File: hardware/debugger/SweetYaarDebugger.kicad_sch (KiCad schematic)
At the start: 21 parts, among them SW1 SW_DPST, U1 USBLC6-2SC6

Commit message: Add schematics
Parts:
- C1: footprint (none) -> Capacitor_SMD:C_0603_1608Metric
- C2, C4: value 4.7u -> 4.7uF; footprint (none) -> Capacitor_SMD:C_0805_2012Metric
- C3, C5: value 100n -> 100nF; footprint (none) -> Capacitor_SMD:C_0603_1608Metric
- J_PROG1: footprint (none) -> Connector_PinHeader_2.54mm:PinHeader_1x06_P2.54mm_Vertical
- R1, R_CC1, R_CC2, R_DTR1, R_RSTb1, R_RTS1, R_VBUS_DIV_BOT1, R_VBUS_DIV_TOP1: footprint (none) -> Resistor_SMD:R_0603_1608Metric
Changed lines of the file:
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@@
 			)
 		)
-		(property "Value" "100n"
+		(property "Value" "100nF"
 			(at 114.554 50.546 0)
 			(show_name no)
@@
 			)
 		)
-		(property "Footprint" ""
+		(property "Footprint" "Capacitor_SMD:C_0603_1608Metric"
 			(at 115.2652 52.07 0)
 			(hide yes)
@@
 			)
 		)
-		(property "Footprint" ""
+		(property "Footprint" "Resistor_SMD:R_0603_1608Metric"
 			(at 167.64 81.28 0)
 			(hide yes)
@@
 			)
 		)
-		(property "Footprint" ""
+		(property "Footprint" "Capacitor_SMD:C_0603_1608Metric"
 			(at 68.58 52.3748 0)
 			(hide yes)
@@
 			)
 		)
-		(property "Footprint" ""
+		(property "Footprint" "Resistor_SMD:R_0603_1608Metric"
 			(at 92.71 78.74 0)
 			(hide yes)
@@
 			)
 		)
-		(property "Footprint" ""
+		(property "Footprint" "Resistor_SMD:R_0603_1608Metric"
 			(at 106.68 62.23 0)
 			(hide yes)
@@
 			)
 		)
-		(property "Footprint" ""
+		(property "Footprint" "Resistor_SMD:R_0603_1608Metric"
 			(at 92.71 71.12 0)
 			(hide yes)
@@
 			)
 		)
-		(property "Value" "4.7u"
+		(property "Value" "4.7uF"
 			(at 106.934 50.546 0)
 			(show_name no)
@@
 			)
 		)
-		(property "Footprint" ""
+		(property "Footprint" "Capacitor_SMD:C_0805_2012Metric"
 			(at 107.6452 52.07 0)
 			(hide yes)
@@
 			)
 		)
-		(property "Footprint" ""
+		(property "Footprint" "Resistor_SMD:R_0603_1608Metric"
 			(at 207.01 62.992 90)
 			(hide yes)
@@
 			)
 		)
-		(property "Footprint" ""
+		(property "Footprint" "Connector_PinHeader_2.54mm:PinHeader_1x06_P2.54mm_Vertical"
 			(at 248.92 73.66 0)
 			(hide yes)
@@
 			)
 		)
-		(property "Footprint" ""
+		(property "Footprint" "Resistor_SMD:R_0603_1608Metric"
 			(at 49.53 53.34 0)
 			(hide yes)
@@
 			)
 		)
-		(property "Footprint" ""
+		(property "Footprint" "Resistor_SMD:R_0603_1608Metric"
 			(at 167.64 67.31 0)
 			(hide yes)
@@
 			)
 		)
-		(property "Footprint" ""
+		(property "Footprint" "Resistor_SMD:R_0603_1608Metric"
 			(at 49.53 50.8 0)
 			(hide yes)
@@
 			)
 		)
-		(property "Value" "100n"
+		(property "Value" "100nF"
 			(at 127.762 50.546 0)
 			(show_name no)
@@
 			)
 		)
-		(property "Footprint" ""
+		(property "Footprint" "Capacitor_SMD:C_0603_1608Metric"
 			(at 127.9652 52.07 0)
 			(hide yes)
@@
 			)
 		)
-		(property "Value" "4.7u"
+		(property "Value" "4.7uF"
 			(at 136.144 50.546 0)
 			(show_name no)
@@
 			)
 		)
-		(property "Footprint" ""
+		(property "Footprint" "Capacitor_SMD:C_0805_2012Metric"
 			(at 136.8552 52.07 0)
 			(hide yes)

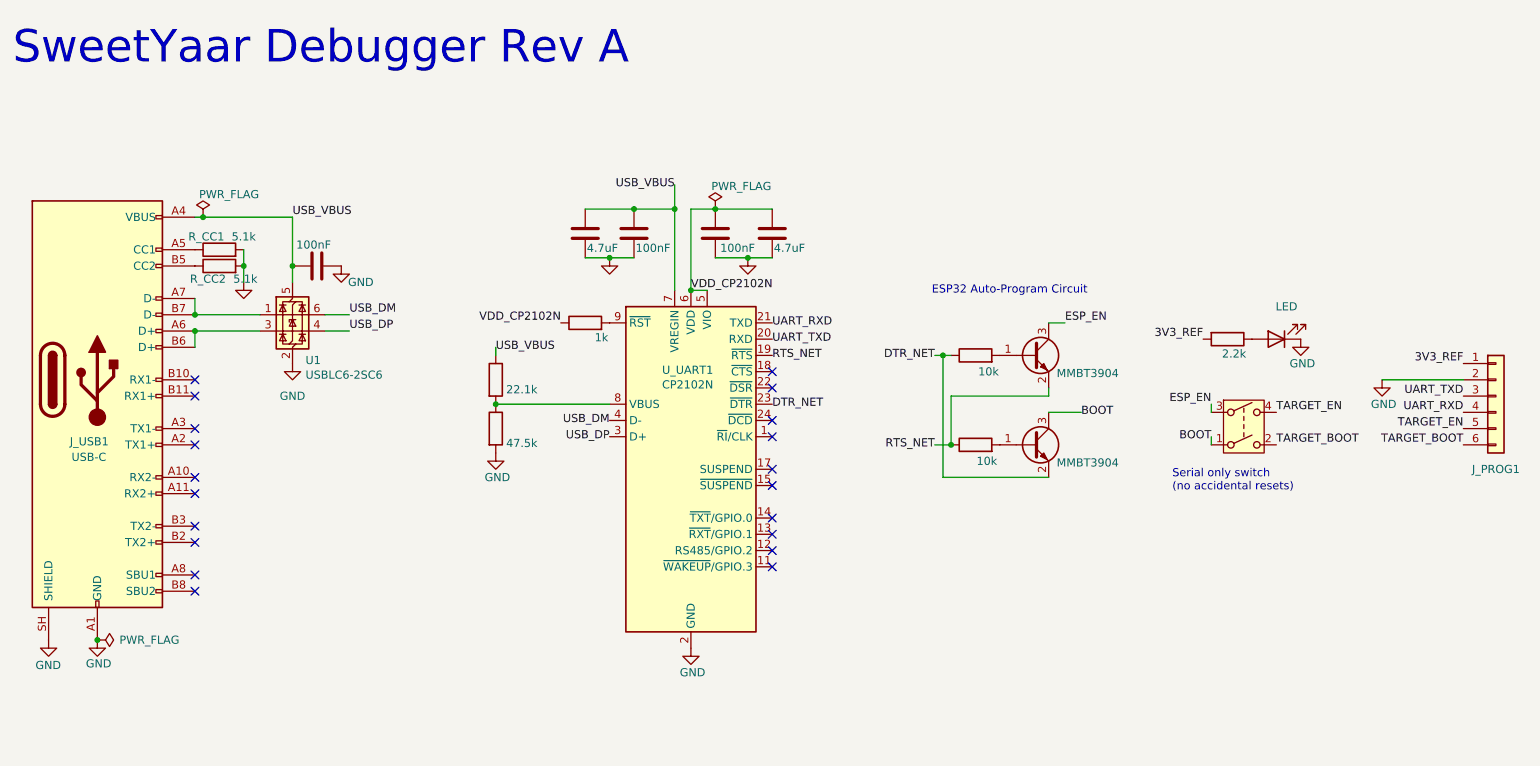
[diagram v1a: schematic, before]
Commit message: changing debugger components to match mainboard
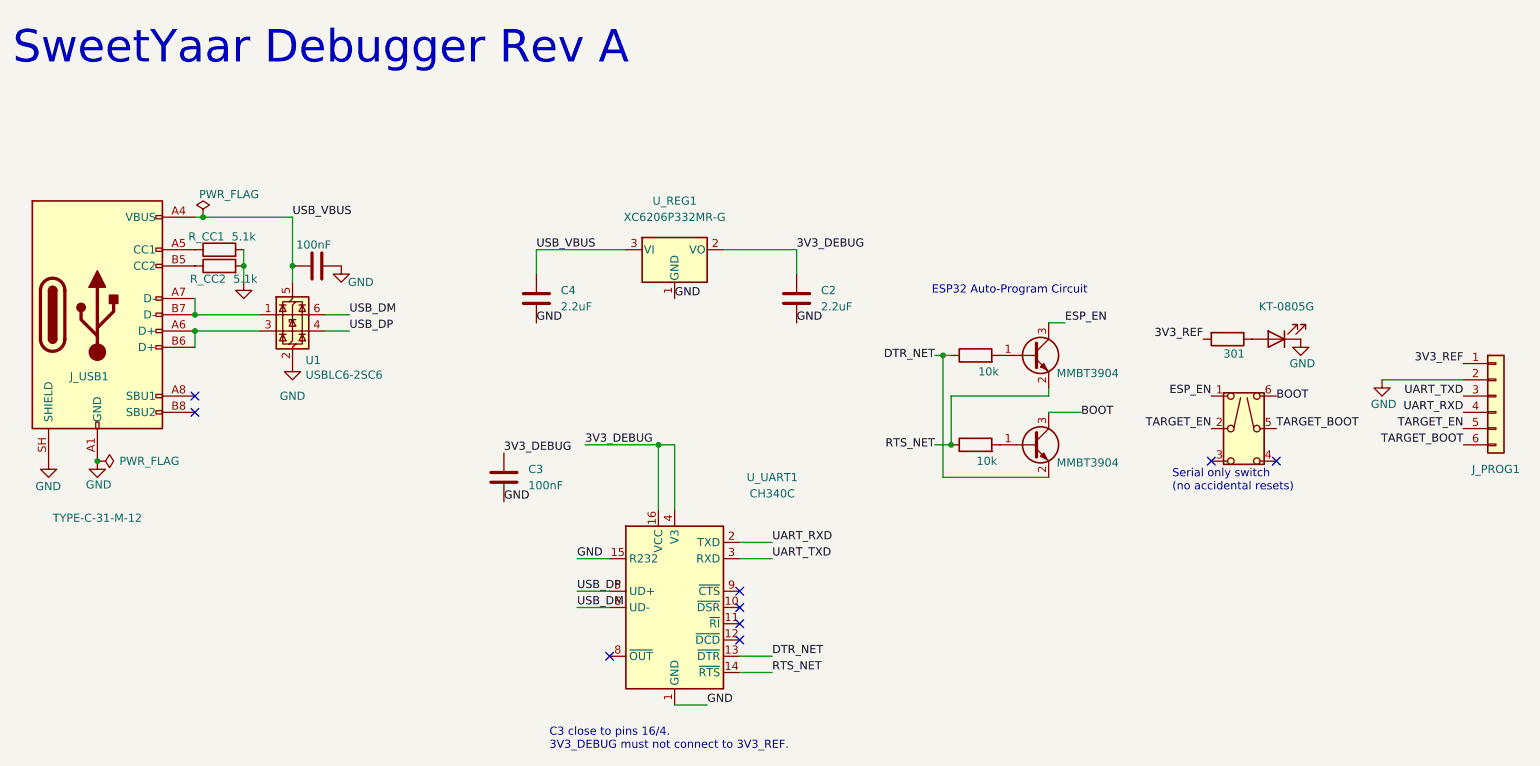
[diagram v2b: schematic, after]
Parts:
- removed C5: 100nF, Capacitor_SMD:C_0603_1608Metric, symbol Device:C
- removed R_RSTb1: 1k, Resistor_SMD:R_0603_1608Metric, symbol Device:R
- removed R_VBUS_DIV_BOT1: 47.5k, Resistor_SMD:R_0603_1608Metric, symbol Device:R
- removed R_VBUS_DIV_TOP1: 22.1k, Resistor_SMD:R_0603_1608Metric, symbol Device:R
- added U_REG1: XC6206P332MR-G, Package_TO_SOT_SMD:SOT-23-3, symbol Regulator_Linear:XC6206PxxxMR
- C1, C3: LCSC (none) -> C14663
- C2, C4: value 4.7uF -> 2.2uF; LCSC (none) -> C126591
- D1: value LED -> KT-0805G; footprint (none) -> LED_SMD:LED_0805_2012Metric; LCSC (none) -> C2297
- J_USB1: value USB-C -> TYPE-C-31-M-12; footprint (none) -> Connector_USB:USB_C_Receptacle_HRO_TYPE-C-31-M-12; symbol Connector:USB_C_Receptacle -> Connector:USB_C_Receptacle_USB2.0_16P; LCSC (none) -> C165948
- Q_DTR1, Q_RTS1: LCSC (none) -> C20526
- R1: value 2.2k -> 301; LCSC (none) -> C25192
- R_CC1, R_CC2: LCSC (none) -> C23186
- R_DTR1, R_RTS1: LCSC (none) -> C25804
- SW1: value SW_DPST -> MS-22D28-G020 (SERIAL ONLY); footprint (none) -> SweetYaar:SW-SMD_MS-22D28-G020; symbol Switch:SW_DPST -> SweetYaar:MS-22D28-G020; LCSC (none) -> C963205
- U_UART1: value CP2102N -> CH340C; footprint (none) -> Package_SO:SOIC-16_3.9x9.9mm_P1.27mm; symbol Interface_USB:CP2102N-Axx-xQFN24 -> SweetYaar:CH340C_3V3; LCSC (none) -> C7464026
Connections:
- net BOOT: now also SW1.6 (C); no longer SW1.1
- net DTR_NET: now also U_UART1.13 (~{DTR}); no longer U_UART1.23 (~{DTR})
- net ESP_EN: now also SW1.1 (A); no longer SW1.3
- net GND: now also U_UART1.1 (GND), U_UART1.15 (R232), U_REG1.1 (GND); no longer U_UART1.2 (GND), U_UART1.25 (GND)
- net RTS_NET: now also U_UART1.14 (~{RTS}); no longer U_UART1.19 (~{RTS})
- net TARGET_BOOT: now also SW1.5 (B); no longer SW1.2
- net TARGET_EN: now also SW1.2 (B); no longer SW1.4
- net UART_RXD: now also U_UART1.2 (TXD); no longer U_UART1.21 (TXD)
- net UART_TXD: now also U_UART1.3 (RXD); no longer U_UART1.20 (RXD)
- net USB_DM: now also U_UART1.6 (UD-); no longer U_UART1.4 (D-)
- net USB_DP: now also U_UART1.5 (UD+); no longer U_UART1.3 (D+)
- net USB_VBUS: now also U_REG1.3 (VI); no longer U_UART1.7 (VREGIN)
- net 3V3_DEBUG: now reaches U_UART1.16 (VCC)
- net 3V3_DEBUG: now also C2.1, C3.1, U_UART1.4 (V3), U_REG1.2 (VO)
- removed net VDD_CP2102N: C2.1, C3.1, U_UART1.5 (VIO), U_UART1.6 (VDD)
- no-connect marks 20 -> 9
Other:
- note added: "C3 close to pins 16/4. 3V3_DEBUG must not connect to 3V3_REF."

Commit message: Add routed debugger PCB and update schematic
Add the fully routed debugger board and its USB and power design rules. Update the schematic and switch documentation, including the 330 ohm LED resistor using LCSC C23138.
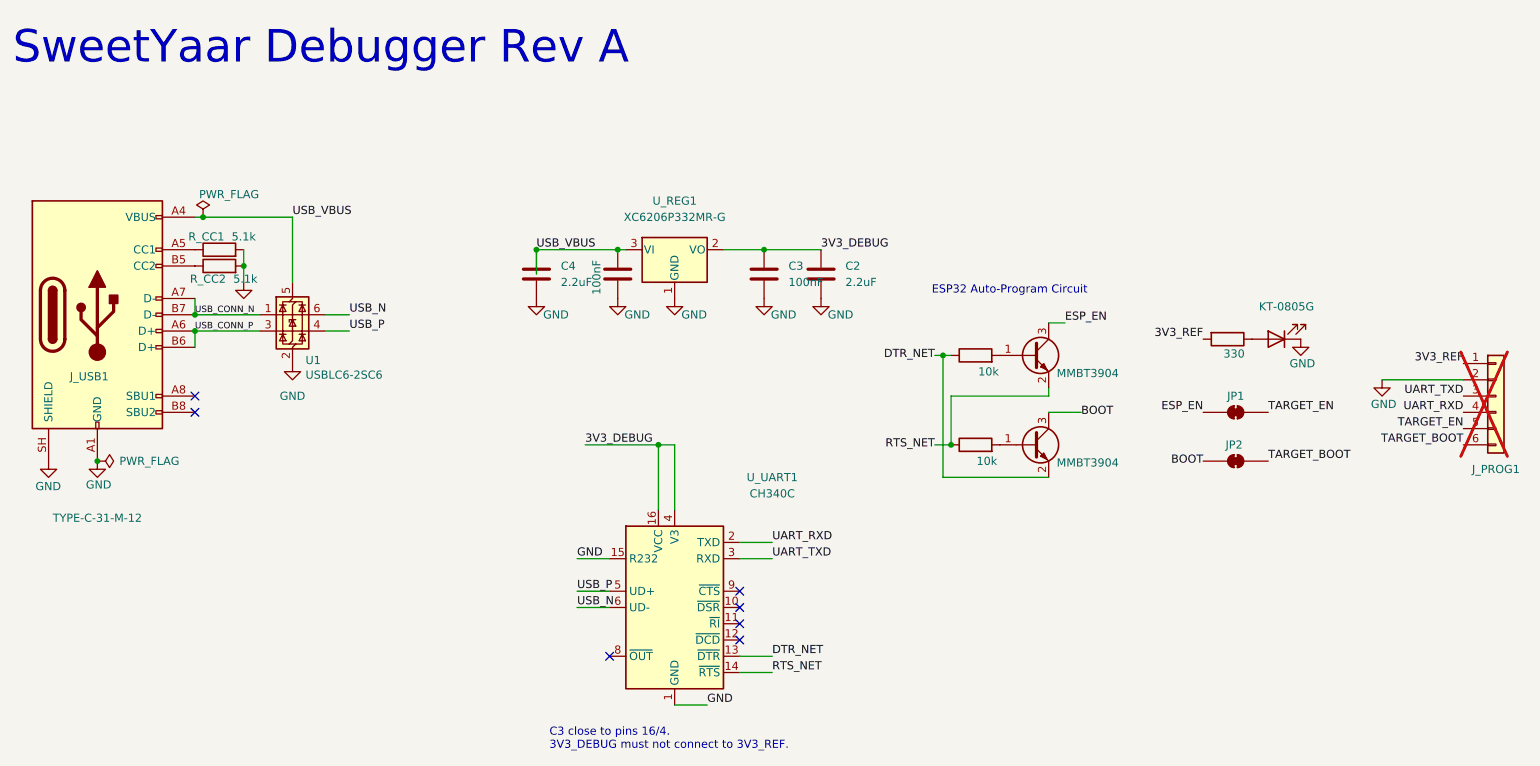
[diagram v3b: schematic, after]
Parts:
- removed SW1: MS-22D28-G020 (SERIAL ONLY), SweetYaar:SW-SMD_MS-22D28-G020, symbol SweetYaar:MS-22D28-G020
- added JP1, JP2: SolderJumper_2_Bridged, Jumper:SolderJumper-2_P1.3mm_Bridged_RoundedPad1.0x1.5mm, symbol Jumper:SolderJumper_2_Bridged
- J_PROG1: now not fitted
- R1: value 301 -> 330; LCSC C25192 -> C23138
- U1: LCSC (none) -> C7519
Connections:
- net BOOT: now also JP2.1 (A)
- net ESP_EN: now also JP1.1 (A)
- net GND: now also C1.1; no longer C1.2
- net TARGET_BOOT: now also JP2.2 (B)
- net TARGET_EN: now also JP1.2 (B)
- net USB_VBUS: now also C1.2; no longer C1.1
- net USB_CONN_P: now reaches J_USB1.A6 (D+), J_USB1.B6 (D+), U1.3 (I/O2)
- net USB_CONN_N: now reaches J_USB1.A7 (D-), J_USB1.B7 (D-), U1.1 (I/O1)
- net USB_DM renamed USB_N
- net USB_DP renamed USB_P
- no-connect marks 9 -> 7
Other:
- note removed: "Serial only switch (no accidental resets)"
- moved on the sheet: C2, C3, C4

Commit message: Fixing rotation and position offsets
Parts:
- J_USB1: footprint Connector_USB:USB_C_Receptacle_HRO_TYPE-C-31-M-12 -> SweetYaar:USB_C_Receptacle_HRO_TYPE-C-31-M-12 - C165948
- U1: footprint Package_TO_SOT_SMD:SOT-23-6 -> SweetYaar:SOT-23-6 - USBLC6-2SC6 - C7519
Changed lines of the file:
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@@
 			)
 		)
-		(property "Footprint" "Connector_USB:USB_C_Receptacle_HRO_TYPE-C-31-M-12"
+		(property "Footprint" "SweetYaar:USB_C_Receptacle_HRO_TYPE-C-31-M-12 - C165948"
 			(at 34.29 60.96 0)
 			(hide yes)
@@
 			)
 		)
-		(property "Footprint" "Package_TO_SOT_SMD:SOT-23-6"
+		(property "Footprint" "SweetYaar:SOT-23-6 - USBLC6-2SC6 - C7519"
 			(at 62.23 67.31 0)
 			(hide yes)

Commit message: Creating production v1.0 manufacturing files
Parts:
- C2, C4: value 2.2uF -> 4.7uF; LCSC C126591 -> C1779
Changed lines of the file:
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@@
-	)
-	(junction
-		(at 99.06 50.8)
-		(diameter 0)
-		(color 0 0 0 0)
 	)
 	(junction
@@
 		(pts
 			(xy 179.07 73.66) (xy 179.07 72.39)
-		)
-		(stroke
-			(width 0)
-			(type default)
-		)
-	)
-	(wire
-		(pts
-			(xy 99.06 50.8) (xy 99.06 54.61)
 		)
 		(stroke
@@
 			)
 		)
-		(property "Value" "2.2uF"
+		(property "Value" "4.7uF"
 			(at 147.32 55.88 0)
 			(show_name no)
@@
 			)
 		)
-		(property "Datasheet" "https://www.lcsc.com/datasheet/C126591.pdf"
+		(property "Datasheet" "https://www.lcsc.com/datasheet/C1779.pdf"
 			(at 143.51 54.61 0)
 			(hide yes)
@@
 			)
 		)
-		(property "LCSC" "C126591"
+		(property "LCSC" "C1779"
 			(at 143.51 54.61 0)
 			(hide yes)
@@
 			)
 		)
-		(property "Value" "2.2uF"
+		(property "Value" "4.7uF"
 			(at 102.87 55.88 0)
 			(show_name no)
@@
 			)
 		)
-		(property "Datasheet" "https://www.lcsc.com/datasheet/C126591.pdf"
+		(property "Datasheet" "https://www.lcsc.com/datasheet/C1779.pdf"
 			(at 99.06 54.61 0)
 			(hide yes)
@@
 			)
 		)
-		(property "LCSC" "C126591"
+		(property "LCSC" "C1779"
 			(at 99.06 54.61 0)
 			(hide yes)
